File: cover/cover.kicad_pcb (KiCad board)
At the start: 2 copper layers, 35.2 x 51.8 mm, 2 parts

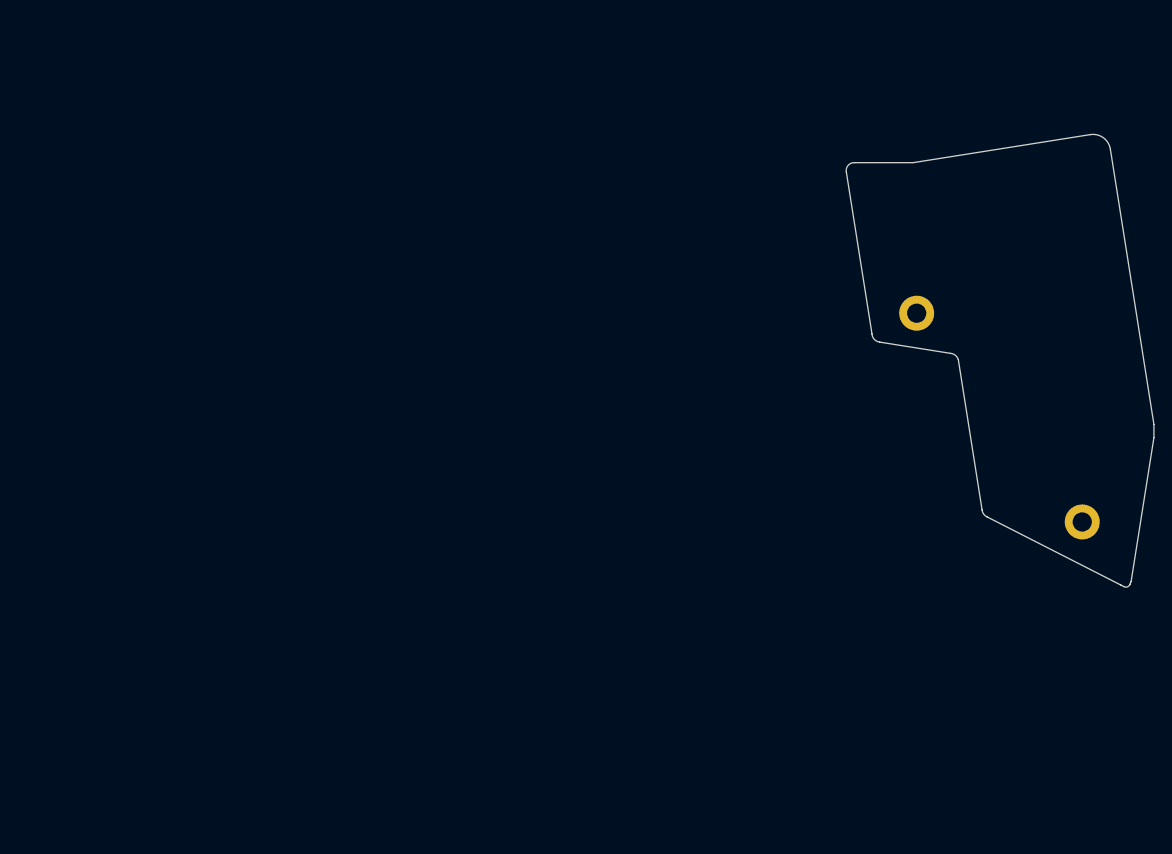
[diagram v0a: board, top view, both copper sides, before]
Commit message: Created cover
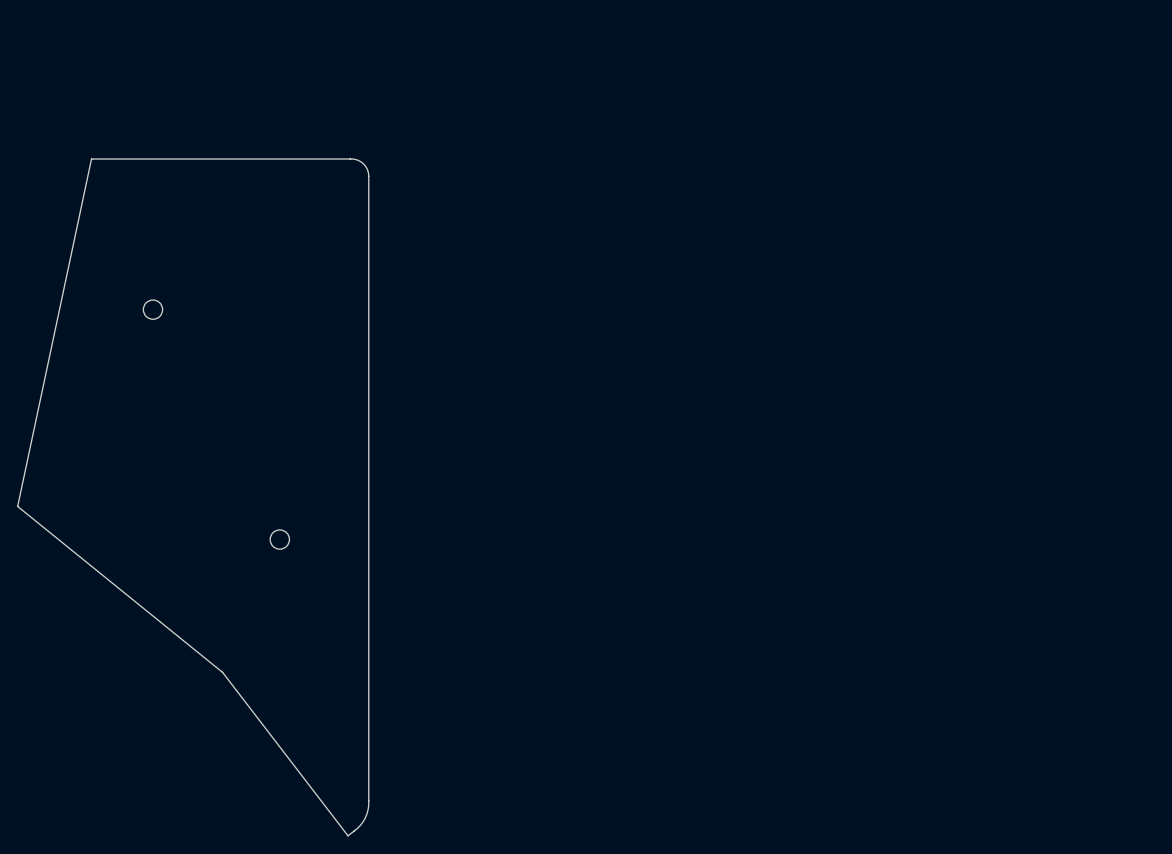
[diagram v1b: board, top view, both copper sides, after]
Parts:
- moved H15 91.8 mm to (154.9, 99.4), turned to 0 degrees
- moved HM12 86.8 mm to (141.0, 74.0), turned to 351 degrees
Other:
- board size 35.2 x 51.8 mm -> 40.2 x 77.4 mm
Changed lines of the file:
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@@
   (general
     (thickness 1.6)
-    (drawings 17)
+    (drawings 21)
     (tracks 0)
     (zones 0)
@@
     (mod_text_size 1 1)
     (mod_text_width 0.15)
-    (pad_size 1.524 1.524)
-    (pad_drill 0.762)
+    (pad_size 2.2 2.2)
+    (pad_drill 2.2)
     (pad_to_mask_clearance 0)
     (aux_axis_origin 0 0)
     (visible_elements FFFFFF7F)
     (pcbplotparams
-      (layerselection 0x010fc_ffffffff)
+      (layerselection 0x010cc_7ffffffe)
       (usegerberextensions false)
       (usegerberattributes true)
@@
       (outputformat 1)
       (mirror false)
-      (drillshape 1)
+      (drillshape 0)
       (scaleselection 1)
       (outputdirectory ""))
@@
   )
   (module used_footprints:M2_HOLE_PCB (layer F.Cu)
-    (at 227.81 73.47)
-    (fp_text reference HM12 (at 0 2.7) (layer F.SilkS) hide
+    (at 154.918781 99.44053)
+    (fp_text reference H15 (at 0 2.7) (layer F.SilkS) hide
       (effects (font (size 1 1) (thickness 0.15)))
     )
-    (fp_text value CaseHole (at 0 -2.6) (layer F.Fab) hide
+    (fp_text value MountingHole (at 0 -2.6) (layer F.Fab) hide
       (effects (font (size 1 1) (thickness 0.15)))
     )
-    (pad "" thru_hole circle (at 0 0) (size 4 4) (drill 2.2) (layers *.Cu *.Mask))
+    (pad "" np_thru_hole circle (at 0.033741 -0.075686) (size 2.2 2.2) (drill 2.2) (layers *.Cu *.Mask))
   )
   (module used_footprints:M2_HOLE_PCB (layer F.Cu)
-    (at 246.7 97.25 9)
-    (fp_text reference H15 (at 0 2.7 9) (layer F.SilkS) hide
+    (at 141.018764 73.953675 351)
+    (fp_text reference HM12 (at 0 2.7 171) (layer F.SilkS) hide
       (effects (font (size 1 1) (thickness 0.15)))
     )
-    (fp_text value MountingHole (at 0 -2.6 9) (layer F.Fab) hide
+    (fp_text value CaseHole (at 0 -2.6 171) (layer F.Fab) hide
       (effects (font (size 1 1) (thickness 0.15)))
     )
-    (pad "" thru_hole circle (at 0.033741 0.106591 9) (size 4 4) (drill 2.2) (layers *.Cu *.Mask))
+    (pad "" np_thru_hole circle (at -0.7079 -0.787792 351) (size 2.2 2.2) (drill 2.2) (layers *.Cu *.Mask))
   )
-  (gr_arc (start 251.748757 104.308975) (end 251.524044 104.75) (angle -99.18619356) (layer Edge.Cuts) (width 0.05))
-  (gr_line (start 251.17 104.57) (end 251.524044 104.75) (layer Edge.Cuts) (width 0.05))
-  (gr_line (start 252.34 104.17) (end 252.22 104.460399) (layer Edge.Cuts) (width 0.05))
-  (gr_line (start 227.4 56.25) (end 220.7 56.25) (layer Edge.Cuts) (width 0.05))
-  (gr_line (start 231.691161 78.065779) (end 223.579911 76.777626) (layer Edge.Cuts) (width 0.05))
-  (gr_arc (start 231.589335 79.090086) (end 232.571916 78.783316) (angle -67) (layer Edge.Cuts) (width 0.05))
-  (gr_arc (start 247.990448 55.013936) (end 249.965825 54.701067) (angle -90) (layer Edge.Cuts) (width 0.05))
-  (gr_arc (start 236.287309 95.864367) (end 235.29 95.97) (angle -58.69438331) (layer Edge.Cuts) (width 0.05))
-  (gr_line (start 232.571916 78.783316) (end 235.29 95.97) (layer Edge.Cuts) (width 0.05))
-  (gr_arc (start 223.697309 75.784367) (end 222.7 75.86) (angle -78.9) (layer Edge.Cuts) (width 0.05))
-  (gr_line (start 254.95 86.2) (end 254.95 87.7) (layer Edge.Cuts) (width 0.05))
-  (gr_arc (start 220.653711 57.156774) (end 220.7 56.25) (angle -105.1713239) (layer Edge.Cuts) (width 0.05))
-  (gr_line (start 249.965825 54.701067) (end 254.95 86.2) (layer Edge.Cuts) (width 0.05))
-  (gr_line (start 247.677579 53.038559) (end 227.4 56.25) (layer Edge.Cuts) (width 0.05))
-  (gr_line (start 219.766426 57.349407) (end 222.7 75.86) (layer Edge.Cuts) (width 0.05))
-  (gr_line (start 235.859358 96.771363) (end 251.17 104.57) (layer Edge.Cuts) (width 0.05))
-  (gr_line (start 254.95 87.7) (end 252.34 104.17) (layer Edge.Cuts) (width 0.05))
+  (gr_line (start 140.442828 78.213677) (end 140.442821 73.06484) (layer Dwgs.User) (width 0.15))
+  (gr_line (start 136.439092 54.07) (end 136.439103 74.963686) (layer Cmts.User) (width 0.15))
+  (gr_line (start 163.396799 132.763936) (end 163.426409 132.737134) (layer Edge.Cuts) (width 0.05))
+  (gr_line (start 162.747693 133.249407) (end 162.75418 133.257034) (layer Edge.Cuts) (width 0.05))
+  (gr_line (start 148.385984 114.544874) (end 148.417444 114.573872) (layer Edge.Cuts) (width 0.05))
+  (gr_line (start 124.965749 95.561957) (end 124.970575 95.583453) (layer Edge.Cuts) (width 0.05))
+  (gr_line (start 133.42 55.83) (end 133.406959 55.849164) (layer Edge.Cuts) (width 0.05))
+  (gr_line (start 163.01 55.83) (end 163.048599 55.831459) (layer Edge.Cuts) (width 0.05))
+  (gr_line (start 133.406959 55.849164) (end 124.965749 95.561957) (layer Edge.Cuts) (width 0.05))
+  (gr_line (start 124.970575 95.583453) (end 148.385984 114.544874) (layer Edge.Cuts) (width 0.05))
+  (gr_line (start 162.75418 133.257034) (end 163.396799 132.763936) (layer Edge.Cuts) (width 0.05))
+  (gr_line (start 148.417444 114.573872) (end 162.747693 133.249407) (layer Edge.Cuts) (width 0.05))
+  (gr_line (start 163.01 55.83) (end 133.42 55.83) (layer Edge.Cuts) (width 0.05))
+  (gr_line (start 165.129104 57.811046) (end 165.129108 129.2772) (layer Edge.Cuts) (width 0.05))
+  (gr_arc (start 163.143662 57.814627) (end 165.129104 57.811046) (angle -92.64101847) (layer Edge.Cuts) (width 0.05))
+  (gr_line (start 136.439103 74.963686) (end 144.439094 81.451039) (layer Cmts.User) (width 0.15))
+  (gr_line (start 144.439094 81.451039) (end 144.439129 96.023669) (layer Cmts.User) (width 0.15))
+  (gr_line (start 144.439129 96.023669) (end 166.169104 113.621008) (layer Cmts.User) (width 0.15))
+  (gr_arc (start 161.154249 129.470013) (end 163.426409 132.737134) (angle -57.95998997) (layer Edge.Cuts) (width 0.05))
+  (gr_line (start 140.442821 73.06484) (end 136.442822 73.064837) (layer Dwgs.User) (width 0.15))
+  (gr_line (start 154.918768 104.513681) (end 154.918772 99.364841) (layer Dwgs.User) (width 0.15))
 )

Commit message: Created the promicro cover
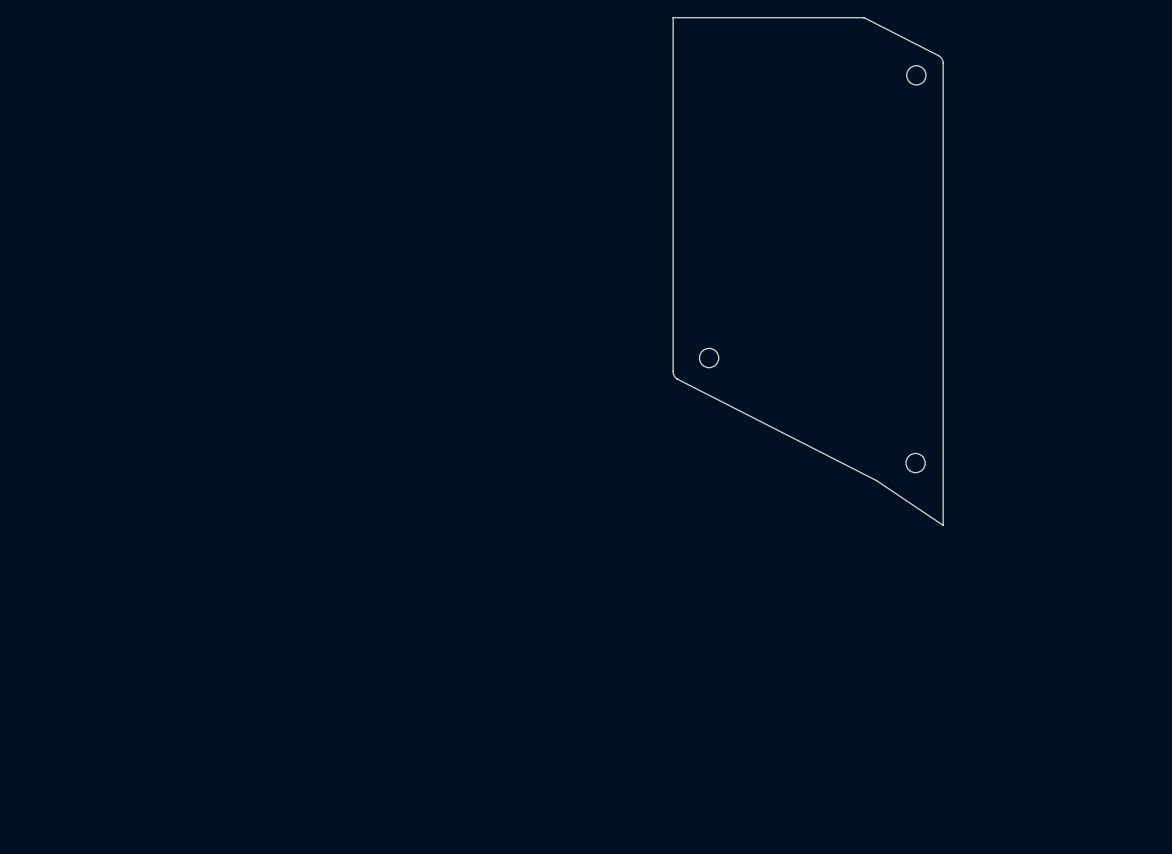
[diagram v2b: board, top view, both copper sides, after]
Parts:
- added HM1: CaseHole, used_footprints:M2_HOLE_PCB, F.Cu at (227.8, 46.3)
- moved H15 73.4 mm to (227.8, 90.7)
- moved HM12 64.0 mm to (204.8, 79.0)
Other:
- board size 40.2 x 77.4 mm -> 30.9 x 58.1 mm
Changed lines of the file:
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@@
   (general
     (thickness 1.6)
-    (drawings 21)
+    (drawings 13)
     (tracks 0)
     (zones 0)
-    (modules 2)
+    (modules 3)
     (nets 1)
   )
@@
   )
   (module used_footprints:M2_HOLE_PCB (layer F.Cu)
-    (at 154.918781 99.44053)
+    (at 227.774957 90.660868)
     (fp_text reference H15 (at 0 2.7) (layer F.SilkS) hide
       (effects (font (size 1 1) (thickness 0.15)))
@@
       (effects (font (size 1 1) (thickness 0.15)))
     )
-    (pad "" np_thru_hole circle (at 0.033741 -0.075686) (size 2.2 2.2) (drill 2.2) (layers *.Cu *.Mask))
+    (pad "" np_thru_hole circle (at -0.089101 -0.045399) (size 2.2 2.2) (drill 2.2) (layers *.Cu *.Mask))
   )
   (module used_footprints:M2_HOLE_PCB (layer F.Cu)
-    (at 141.018764 73.953675 351)
+    (at 204.774958 78.960866 351)
     (fp_text reference HM12 (at 0 2.7 171) (layer F.SilkS) hide
       (effects (font (size 1 1) (thickness 0.15)))
@@
       (effects (font (size 1 1) (thickness 0.15)))
     )
-    (pad "" np_thru_hole circle (at -0.7079 -0.787792 351) (size 2.2 2.2) (drill 2.2) (layers *.Cu *.Mask))
+    (pad "" np_thru_hole circle (at -0.760845 -0.247214 351) (size 2.2 2.2) (drill 2.2) (layers *.Cu *.Mask))
   )
-  (gr_line (start 140.442828 78.213677) (end 140.442821 73.06484) (layer Dwgs.User) (width 0.15))
-  (gr_line (start 136.439092 54.07) (end 136.439103 74.963686) (layer Cmts.User) (width 0.15))
-  (gr_line (start 163.396799 132.763936) (end 163.426409 132.737134) (layer Edge.Cuts) (width 0.05))
-  (gr_line (start 162.747693 133.249407) (end 162.75418 133.257034) (layer Edge.Cuts) (width 0.05))
-  (gr_line (start 148.385984 114.544874) (end 148.417444 114.573872) (layer Edge.Cuts) (width 0.05))
-  (gr_line (start 124.965749 95.561957) (end 124.970575 95.583453) (layer Edge.Cuts) (width 0.05))
-  (gr_line (start 133.42 55.83) (end 133.406959 55.849164) (layer Edge.Cuts) (width 0.05))
-  (gr_line (start 163.01 55.83) (end 163.048599 55.831459) (layer Edge.Cuts) (width 0.05))
-  (gr_line (start 133.406959 55.849164) (end 124.965749 95.561957) (layer Edge.Cuts) (width 0.05))
-  (gr_line (start 124.970575 95.583453) (end 148.385984 114.544874) (layer Edge.Cuts) (width 0.05))
-  (gr_line (start 162.75418 133.257034) (end 163.396799 132.763936) (layer Edge.Cuts) (width 0.05))
-  (gr_line (start 148.417444 114.573872) (end 162.747693 133.249407) (layer Edge.Cuts) (width 0.05))
-  (gr_line (start 163.01 55.83) (end 133.42 55.83) (layer Edge.Cuts) (width 0.05))
-  (gr_line (start 165.129104 57.811046) (end 165.129108 129.2772) (layer Edge.Cuts) (width 0.05))
-  (gr_arc (start 163.143662 57.814627) (end 165.129104 57.811046) (angle -92.64101847) (layer Edge.Cuts) (width 0.05))
-  (gr_line (start 136.439103 74.963686) (end 144.439094 81.451039) (layer Cmts.User) (width 0.15))
-  (gr_line (start 144.439094 81.451039) (end 144.439129 96.023669) (layer Cmts.User) (width 0.15))
-  (gr_line (start 144.439129 96.023669) (end 166.169104 113.621008) (layer Cmts.User) (width 0.15))
-  (gr_arc (start 161.154249 129.470013) (end 163.426409 132.737134) (angle -57.95998997) (layer Edge.Cuts) (width 0.05))
-  (gr_line (start 140.442821 73.06484) (end 136.442822 73.064837) (layer Dwgs.User) (width 0.15))
-  (gr_line (start 154.918768 104.513681) (end 154.918772 99.364841) (layer Dwgs.User) (width 0.15))
+  (module used_footprints:M2_HOLE_PCB (layer F.Cu)
+    (at 227.774961 46.260876 340.5)
+    (fp_text reference HM1 (at 0 2.7 160.5) (layer F.SilkS) hide
+      (effects (font (size 1 1) (thickness 0.15)))
+    )
+    (fp_text value CaseHole (at 0 -2.6 160.5) (layer F.Fab) hide
+      (effects (font (size 1 1) (thickness 0.15)))
+    )
+    (pad "" np_thru_hole circle (at 0 0 340.5) (size 2.2 2.2) (drill 2.2) (layers *.Cu *.Mask))
+  )
+  (gr_line (start 199.96 39.665044) (end 199.947878 39.68) (layer Edge.Cuts) (width 0.05))
+  (gr_line (start 200.074958 80.160872) (end 252.19884 106.719313) (layer Cmts.User) (width 0.15))
+  (gr_line (start 200.77496 81.560868) (end 201.074961 59.060882) (layer Cmts.User) (width 0.15))
+  (gr_arc (start 200.950259 80.154978) (end 199.94788 80.113509) (angle -59.3) (layer Edge.Cuts) (width 0.05))
+  (gr_line (start 223.218253 92.621212) (end 230.842242 97.746664) (layer Edge.Cuts) (width 0.05))
+  (gr_circle (center 212.72 58.36) (end 212.844683 58.531638) (layer Cmts.User) (width 0.15))
+  (gr_arc (start 229.846502 44.887434) (end 230.841843 44.852134) (angle -60.24128881) (layer Edge.Cuts) (width 0.05))
+  (gr_line (start 221.806128 39.671713) (end 230.309896 44.005835) (layer Edge.Cuts) (width 0.05))
+  (gr_line (start 200.40354 80.996157) (end 223.218253 92.621212) (layer Edge.Cuts) (width 0.05))
+  (gr_line (start 221.737224 39.66504) (end 199.96 39.665044) (layer Edge.Cuts) (width 0.05))
+  (gr_line (start 199.94788 80.113509) (end 199.947878 39.68) (layer Edge.Cuts) (width 0.05))
+  (gr_line (start 221.737224 39.66504) (end 221.806128 39.671713) (layer Edge.Cuts) (width 0.05))
+  (gr_line (start 230.841843 44.852134) (end 230.842242 97.746664) (layer Edge.Cuts) (width 0.05))
 )
